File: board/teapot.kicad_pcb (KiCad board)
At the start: 2 copper layers, 50 x 50 mm, 41 parts, among them P1 BATT, P2 SMA, Q1 TEPT4400, U1 TPS79333DBVR, U2 TLV61225, U3 microusb-b, U4 RFM69W, U5 STM32L052K8, U6 HTU21D, U7 MS5637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

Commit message: Setup boardhouse capabilities, track/via spec
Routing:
- net +3V3: track 184.6 -> 0.00 mm
- net GND: track 93.0 -> 0.00 mm, vias 21 -> 0
- net /I2C_SCK: track 53.0 -> 0.00 mm, vias 4 -> 0
- net /I2C_SDA: track 33.9 -> 0.00 mm, vias 2 -> 0
- net /RFM_SCK: track 29.8 -> 0.00 mm, vias 2 -> 0
- net /nRST: track 29.1 -> 0.00 mm, vias 2 -> 0
- net /RFM_MISO: track 28.9 -> 0.00 mm, vias 2 -> 0
- net /RFM_MOSI: track 27.8 -> 0.00 mm, vias 2 -> 0
- net Net-(C1-Pad1): track 27.4 -> 0.00 mm, vias 2 -> 0
- net /RFM_NSS: track 27.1 -> 0.00 mm, vias 2 -> 0
- net /LIGHT_SENSE: track 25.0 -> 0.00 mm, vias 2 -> 0
- net /LIGHT_EN: track 24.8 -> 0.00 mm, vias 2 -> 0
- net /RFM_RESET: track 14.1 -> 0.00 mm, vias 2 -> 0
- net /SWDIO: track 12.7 -> 0.00 mm
- net /SWCLK: track 12.2 -> 0.00 mm
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- removed copper zone on F.Cu, net +3V3
- removed copper zone on B.Cu, net GND
- removed copper zone on F.Cu, net GND
- removed copper zone on F.Cu, net Net-(C1-Pad1)
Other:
- net class Default: clearance 0.1 -> 0.2; via_dia 1.2 -> 0.7; via_drill 0.6 -> 0.3
- rule trace_clearance: 0.1 -> 0.2
- rule trace_min: 0.25 -> 0.2
- rule via_min_drill: 0.2 -> 0.3
- rule via_min_size: 0.8 -> 0.7

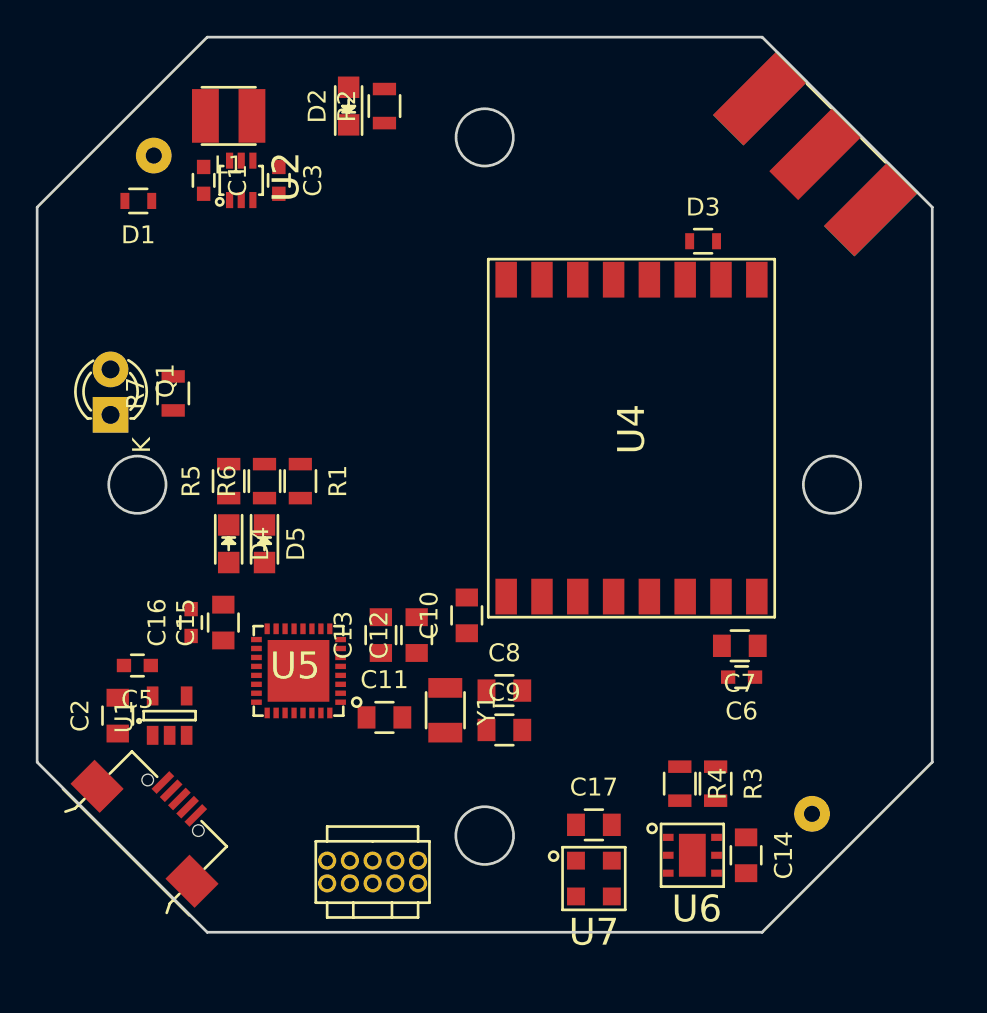
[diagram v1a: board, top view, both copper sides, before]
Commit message: Changed to agg's microusb-ab connector
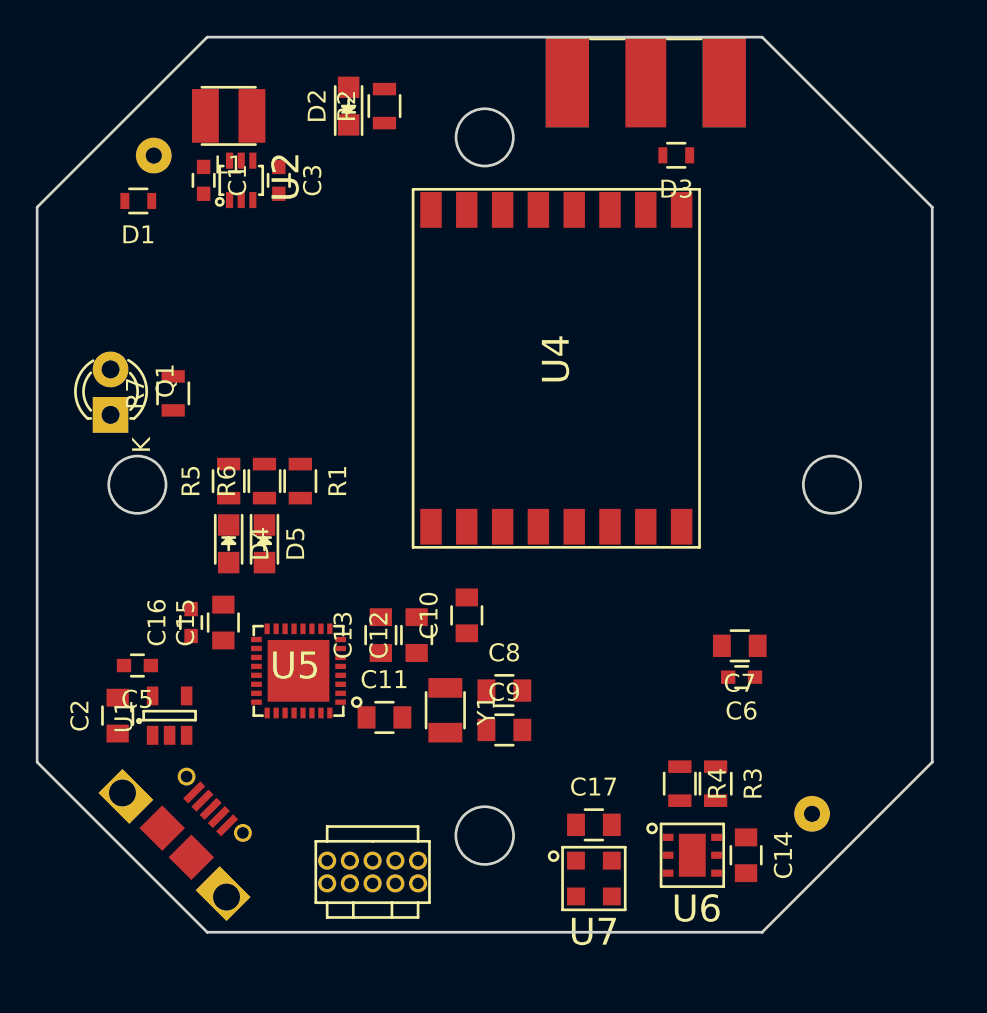
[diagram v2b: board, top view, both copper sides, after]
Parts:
- removed U3: microusb-b, footprints:USB3065
- added J1: MICROUSB, agg:MICROUSB_MOLEX_47589-0001, F.Cu at (109.8, 133.0)
- moved P2 10.3 mm to (136.0, 90.5), turned to 0 degrees
- moved U4 5.73 mm to (131.0, 106.5)
- moved D3 5.03 mm to (137.7, 94.6), turned to 180 degrees
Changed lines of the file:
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@@
 (kicad_pcb (version 4) (host pcbnew 4.0.1-3.201512150931+6195~38~ubuntu14.04.1-stable)
   (general
-    (links 104)
-    (no_connects 104)
-    (area 100.562048 86.662048 153.237952 139.337952)
+    (links 109)
+    (no_connects 109)
+    (area 101.924999 87.924999 152.075001 138.075001)
     (thickness 1.6)
     (drawings 16)
@@
     (zones 0)
     (modules 41)
-    (nets 29)
+    (nets 30)
   )
   (page A4)
@@
   (net 27 /BATT_MON)
   (net 28 /RFM_RESET)
+  (net 29 "Net-(J1-PadS)")
   (net_class Default "This is the default net class."
     (clearance 0.2)
@@
     (add_net "Net-(D4-Pad1)")
     (add_net "Net-(D5-Pad1)")
+    (add_net "Net-(J1-PadS)")
     (add_net "Net-(L1-Pad2)")
   )
@@
   )
   (module footprints:RFM69 (layer F.Cu)
-    (at 135.2 110.4 90)
+    (at 131 106.5 90)
     (fp_text reference U4 (at 0.5 0 90) (layer F.SilkS)
       (effects (font (size 1.5 1.5) (thickness 0.15)))
@@
   )
   (module footprints:SMA-142-0701-801 (layer F.Cu)
-    (at 145.5 94.5 315)
-    (fp_text reference P2 (at 0 -4.064 315) (layer F.SilkS) hide
-      (effects (font (size 1 1) (thickness 0.15)))
-    )
-    (fp_text value SMA (at -3.556 3.81 315) (layer F.SilkS) hide
+    (at 136 90.5)
+    (fp_text reference P2 (at 0 -4.064) (layer F.SilkS) hide
+      (effects (font (size 1 1) (thickness 0.15)))
+    )
+    (fp_text value SMA (at -3.556 3.81) (layer F.SilkS) hide
       (effects (font (size 1 1) (thickness 0.15)))
     )
     (fp_line (start 1.2 -2.4) (end 3.1 -2.4) (layer F.SilkS) (width 0.15))
     (fp_line (start -3.1 -2.4) (end -1.2 -2.4) (layer F.SilkS) (width 0.15))
-    (pad 1 smd rect (at 0 0 315) (size 2.286 5.08) (layers F.Cu F.Mask)
+    (pad 1 smd rect (at 0 0) (size 2.286 5.08) (layers F.Cu F.Mask)
       (net 16 "Net-(D3-Pad2)") (clearance 0.2) (zone_connect 2))
-    (pad 2 smd rect (at -4.3815 0 315) (size 2.413 5.08) (layers F.Cu F.Mask)
+    (pad 2 smd rect (at -4.3815 0) (size 2.413 5.08) (layers F.Cu F.Mask)
       (net 3 GND) (zone_connect 1) (thermal_width 0.5) (thermal_gap 0.2))
-    (pad 3 smd rect (at 4.3815 0 315) (size 2.413 5.08) (layers F.Cu F.Mask)
+    (pad 3 smd rect (at 4.3815 0) (size 2.413 5.08) (layers F.Cu F.Mask)
       (net 3 GND) (zone_connect 1) (thermal_width 0.5) (thermal_gap 0.2))
-    (pad 4 smd rect (at -4.3815 0 315) (size 2.413 5.08) (layers B.Cu B.Mask)
+    (pad 4 smd rect (at -4.3815 0) (size 2.413 5.08) (layers B.Cu B.Mask)
       (net 3 GND) (zone_connect 1) (thermal_width 0.5) (thermal_gap 0.2))
-    (pad 5 smd rect (at 4.3815 0 315) (size 2.413 5.08) (layers B.Cu B.Mask)
+    (pad 5 smd rect (at 4.3815 0) (size 2.413 5.08) (layers B.Cu B.Mask)
       (net 3 GND) (zone_connect 1) (thermal_width 0.5) (thermal_gap 0.2))
   )
@@
     )
   )
-  (module footprints:USB3065 (layer F.Cu)
-    (at 108 132.5 315)
-    (fp_text reference U3 (at -5.656854 -2.12132 315) (layer F.SilkS) hide
-      (effects (font (size 1.5 1.5) (thickness 0.15)))
-    )
-    (fp_text value microusb-b (at 0 -4.75 315) (layer F.Fab) hide
-      (effects (font (size 1.5 1.5) (thickness 0.15)))
-    )
-    (fp_line (start 3.75 1) (end 3.75 1.75) (layer F.SilkS) (width 0.15))
-    (fp_line (start 3.75 1.75) (end 4 2.25) (layer F.SilkS) (width 0.15))
-    (fp_line (start -3.75 1) (end -3.75 1.75) (layer F.SilkS) (width 0.15))
-    (fp_line (start -3.75 1.75) (end -4 2.25) (layer F.SilkS) (width 0.15))
-    (fp_line (start 1.75 -2.75) (end 3.75 -2.75) (layer F.SilkS) (width 0.15))
-    (fp_line (start 3.75 -2.75) (end 3.75 -1) (layer F.SilkS) (width 0.15))
-    (fp_line (start -3.75 -1) (end -3.75 -2.75) (layer F.SilkS) (width 0.15))
-    (fp_line (start -3.75 -2.75) (end -1.75 -2.75) (layer F.SilkS) (width 0.15))
-    (fp_line (start -5 1.45) (end 5 1.45) (layer F.SilkS) (width 0.15))
-    (pad 1 smd rect (at -1.3 -2.75 315) (size 0.4 1.4) (layers F.Cu F.Paste F.Mask)
-      (net 9 +5V))
-    (pad 2 smd rect (at -0.65 -2.75 315) (size 0.4 1.4) (layers F.Cu F.Paste F.Mask)
-      (net 10 /USB_DM))
-    (pad 3 smd rect (at 0 -2.75 315) (size 0.4 1.4) (layers F.Cu F.Paste F.Mask)
-      (net 11 /USB_DP))
-    (pad 4 smd rect (at 0.65 -2.75 315) (size 0.4 1.4) (layers F.Cu F.Paste F.Mask))
-    (pad 5 smd rect (at 1.3 -2.75 315) (size 0.4 1.4) (layers F.Cu F.Paste F.Mask)
-      (net 3 GND))
-    (pad "" np_thru_hole circle (at -2 -2.25 315) (size 0.65 0.65) (drill 0.65) (layers *.Cu *.Mask F.SilkS))
-    (pad "" np_thru_hole circle (at 2 -2.25 315) (size 0.65 0.65) (drill 0.65) (layers *.Cu *.Mask F.SilkS))
-    (pad 6 smd rect (at -3.75 0 315) (size 2.3 1.9) (layers F.Cu F.Paste F.Mask))
-    (pad 7 smd rect (at 3.75 0 315) (size 2.3 1.9) (layers F.Cu F.Paste F.Mask))
-  )
   (module Capacitors_SMD:C_0603 (layer F.Cu)
     (at 111.3 96 270)
@@
   )
   (module Resistors_SMD:R_0603 (layer F.Cu)
-    (at 139.2 99.4)
+    (at 137.7 94.6 180)
     (descr "Resistor SMD 0603, reflow soldering, Vishay (see dcrcw.pdf)")
     (tags "resistor 0603")
     (attr smd)
-    (fp_text reference D3 (at 0 -1.9) (layer F.SilkS)
-      (effects (font (size 1 1) (thickness 0.15)))
-    )
-    (fp_text value TVS_small (at 0 1.9) (layer F.Fab)
+    (fp_text reference D3 (at 0 -1.9 180) (layer F.SilkS)
+      (effects (font (size 1 1) (thickness 0.15)))
+    )
+    (fp_text value TVS_small (at 0 1.9 180) (layer F.Fab)
       (effects (font (size 1 1) (thickness 0.15)))
     )
@@
     (fp_line (start 0.5 0.675) (end -0.5 0.675) (layer F.SilkS) (width 0.15))
     (fp_line (start -0.5 -0.675) (end 0.5 -0.675) (layer F.SilkS) (width 0.15))
-    (pad 1 smd rect (at -0.75 0) (size 0.5 0.9) (layers F.Cu F.Paste F.Mask)
-      (net 3 GND))
-    (pad 2 smd rect (at 0.75 0) (size 0.5 0.9) (layers F.Cu F.Paste F.Mask)
+    (pad 1 smd rect (at -0.75 0 180) (size 0.5 0.9) (layers F.Cu F.Paste F.Mask)
+      (net 3 GND))
+    (pad 2 smd rect (at 0.75 0 180) (size 0.5 0.9) (layers F.Cu F.Paste F.Mask)
       (net 16 "Net-(D3-Pad2)"))
     (model Resistors_SMD.3dshapes/R_0603.wrl
@@
     )
   )
+  (module agg:MICROUSB_MOLEX_47589-0001 (layer F.Cu)
+    (at 109.8 133 45)
+    (fp_text reference J1 (at 0 -6.1 45) (layer F.Fab)
+      (effects (font (size 1 1) (thickness 0.15)))
+    )
+    (fp_text value MICROUSB (at 0 6.2 45) (layer F.Fab)
+      (effects (font (size 1 1) (thickness 0.15)))
+    )
+    (fp_line (start 4 5.5) (end 4 -5.5) (layer F.CrtYd) (width 0.01))
+    (fp_line (start -2.8 5.5) (end 4 5.5) (layer F.CrtYd) (width 0.01))
+    (fp_line (start -2.8 -5.5) (end -2.8 5.5) (layer F.CrtYd) (width 0.01))
+    (fp_line (start 4 -5.5) (end -2.8 -5.5) (layer F.CrtYd) (width 0.01))
+    (fp_line (start 0.29 4.05) (end 0.29 3.75) (layer F.Fab) (width 0.01))
+    (fp_line (start -0.56 4.05) (end 0.29 4.05) (layer F.Fab) (width 0.01))
+    (fp_line (start -0.56 3.75) (end -0.56 4.05) (layer F.Fab) (width 0.01))
+    (fp_line (start 0.29 -4.05) (end 0.29 -3.75) (layer F.Fab) (width 0.01))
+    (fp_line (start -0.56 -4.05) (end 0.29 -4.05) (layer F.Fab) (width 0.01))
+    (fp_line (start -0.56 -4.05) (end -0.56 -3.75) (layer F.Fab) (width 0.01))
+    (fp_line (start -2.76 4.1) (end -2.16 3.75) (layer F.Fab) (width 0.01))
+    (fp_line (start -2.76 -4.1) (end -2.16 -3.75) (layer F.Fab) (width 0.01))
+    (fp_line (start 3.14 2.4) (end 2.94 2.4) (layer F.Fab) (width 0.01))
+    (fp_line (start 3.14 2) (end 3.14 2.4) (layer F.Fab) (width 0.01))
+    (fp_line (start 2.94 2) (end 3.14 2) (layer F.Fab) (width 0.01))
+    (fp_line (start 3.14 -2.45) (end 2.94 -2.45) (layer F.Fab) (width 0.01))
+    (fp_line (start 3.14 -2) (end 3.14 -2.45) (layer F.Fab) (width 0.01))
+    (fp_line (start 2.94 -2) (end 3.14 -2) (layer F.Fab) (width 0.01))
+    (fp_line (start 2.94 3.75) (end -2.16 3.75) (layer F.Fab) (width 0.01))
+    (fp_line (start 2.94 -3.75) (end 2.94 3.75) (layer F.Fab) (width 0.01))
+    (fp_line (start -2.16 -3.75) (end 2.94 -3.75) (layer F.Fab) (width 0.01))
+    (fp_line (start -2.16 -3.75) (end -2.16 3.75) (layer F.Fab) (width 0.01))
+    (fp_line (start -1.46 -5.26) (end -1.46 5.26) (layer F.Fab) (width 0.01))
+    (pad 1 smd rect (at 2.675 -1.3 45) (size 1.35 0.4) (layers F.Cu F.Paste F.Mask)
+      (net 9 +5V))
+    (pad 2 smd rect (at 2.675 -0.65 45) (size 1.35 0.4) (layers F.Cu F.Paste F.Mask)
+      (net 10 /USB_DM))
+    (pad 3 smd rect (at 2.675 0 45) (size 1.35 0.4) (layers F.Cu F.Paste F.Mask)
+      (net 11 /USB_DP))
+    (pad 4 smd rect (at 2.675 0.65 45) (size 1.35 0.4) (layers F.Cu F.Paste F.Mask))
+    (pad 5 smd rect (at 2.675 1.3 45) (size 1.35 0.4) (layers F.Cu F.Paste F.Mask)
+      (net 3 GND))
+    (pad S thru_hole circle (at 3 -2.225 45) (size 1 1) (drill 0.65) (layers *.Cu *.Mask)
+      (net 29 "Net-(J1-PadS)"))
+    (pad S thru_hole circle (at 3 2.225 45) (size 1 1) (drill 0.65) (layers *.Cu *.Mask)
+      (net 29 "Net-(J1-PadS)"))
+    (pad S smd rect (at 0 -1.15 45) (size 1.8 1.8) (layers F.Cu F.Paste F.Mask)
+      (net 29 "Net-(J1-PadS)") (solder_paste_margin -0.3))
+    (pad S smd rect (at 0 1.15 45) (size 1.8 1.8) (layers F.Cu F.Paste F.Mask)
+      (net 29 "Net-(J1-PadS)") (solder_paste_margin -0.3))
+    (pad S thru_hole rect (at -0.18 4.11 225) (size 1.9 2.44) (drill 1.5 (offset 0 0.27)) (layers *.Cu *.Mask F.SilkS)
+      (net 29 "Net-(J1-PadS)"))
+    (pad S thru_hole rect (at -0.18 -4.11 45) (size 1.9 2.44) (drill 1.5 (offset 0 0.27)) (layers *.Cu *.Mask F.SilkS)
+      (net 29 "Net-(J1-PadS)"))
+  )
   (gr_circle (center 146.4 113) (end 148.8 113) (layer F.CrtYd) (width 0.2))

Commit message: New test placement with smaller pcb outline
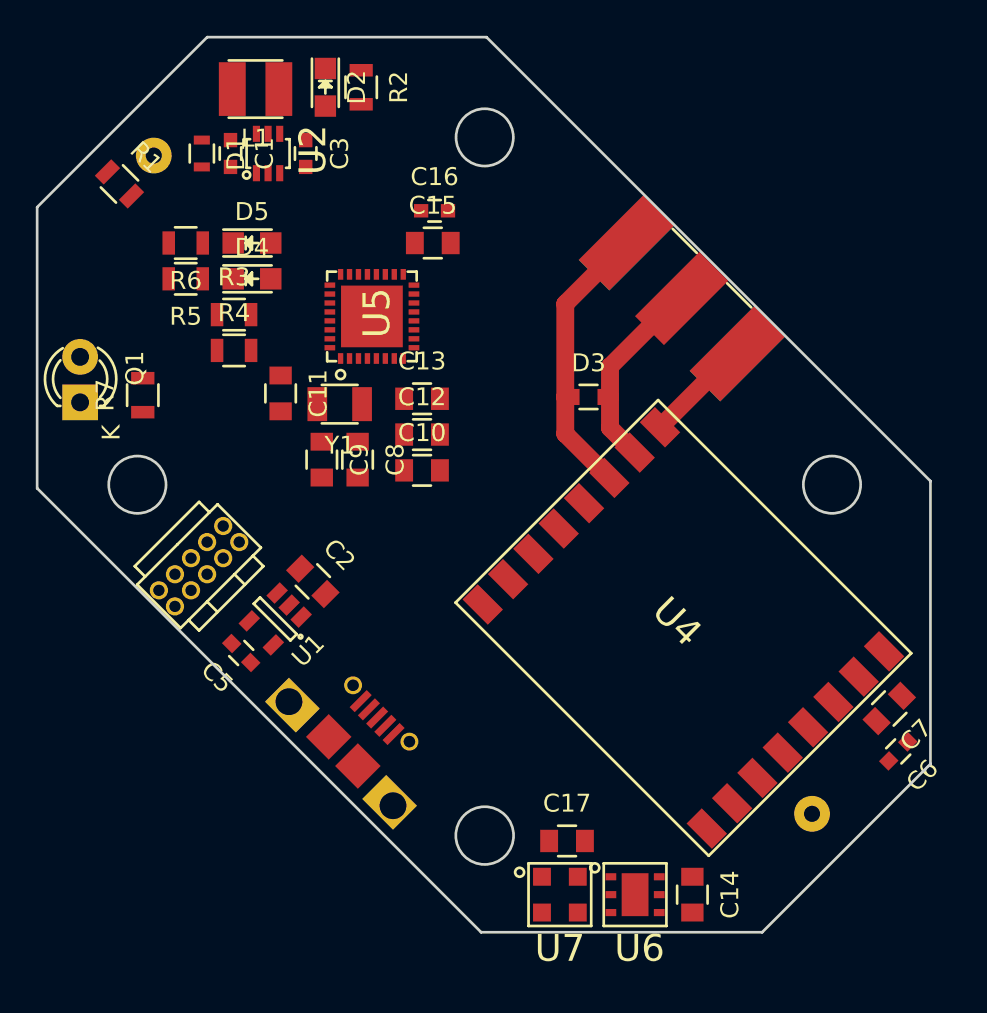
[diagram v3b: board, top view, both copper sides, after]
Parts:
- moved R3 37.6 mm to (113.0, 103.5), turned to 0 degrees
- moved R4 34.7 mm to (113.0, 105.5), turned to 0 degrees
- moved C16 26.7 mm to (124.2, 97.7), turned to 0 degrees
- moved C15 24.2 mm to (124.1, 99.5), turned to 0 degrees
- moved U5 20.2 mm to (120.7, 103.6), turned to 90 degrees
- moved R1 19.4 mm to (106.6, 96.2), turned to 315 degrees
- moved C11 19.0 mm to (115.6, 107.9), turned to 270 degrees
- moved C9 18.2 mm to (117.9, 111.6), turned to 270 degrees
- moved Y1 18.1 mm to (118.9, 108.5), turned to 180 degrees
- moved U8 17.8 mm to (108.8, 118.9), turned to 45 degrees
- moved D5 16.8 mm to (114.0, 99.5), turned to 0 degrees
- moved U4 16.1 mm to (138.1, 121.0), turned to 135 degrees
- moved C8 15.3 mm to (119.9, 111.6), turned to 270 degrees
- moved D4 14.9 mm to (114.0, 101.5), turned to 0 degrees
- moved D3 14.4 mm to (132.8, 108.1), turned to 0 degrees
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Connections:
- U5 pad 15: /LED_YELLOW -> (no net)
- U5 pad 16: /LED_GREEN -> (no net)
- U5 pad 25: (no net) -> /LED_GREEN
- U5 pad 26: (no net) -> /LED_YELLOW
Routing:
- net GND: track 0.00 -> 22.4 mm
- net Net-(D3-Pad2): track 0.00 -> 11.9 mm
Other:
- board size 50 x 50 mm -> 49.9 x 50 mm
